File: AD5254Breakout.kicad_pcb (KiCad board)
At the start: 2 copper layers, 20.6 x 18 mm, 13 parts, among them J1 Conn_01x08, J2 Conn_01x08, U1 AD5254

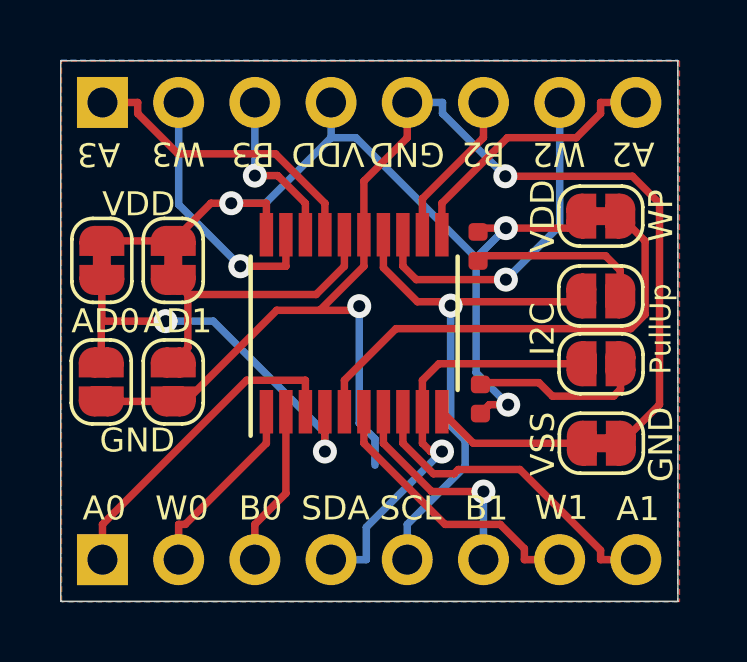
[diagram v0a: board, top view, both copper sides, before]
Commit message: Add condensor as Rev2021.05
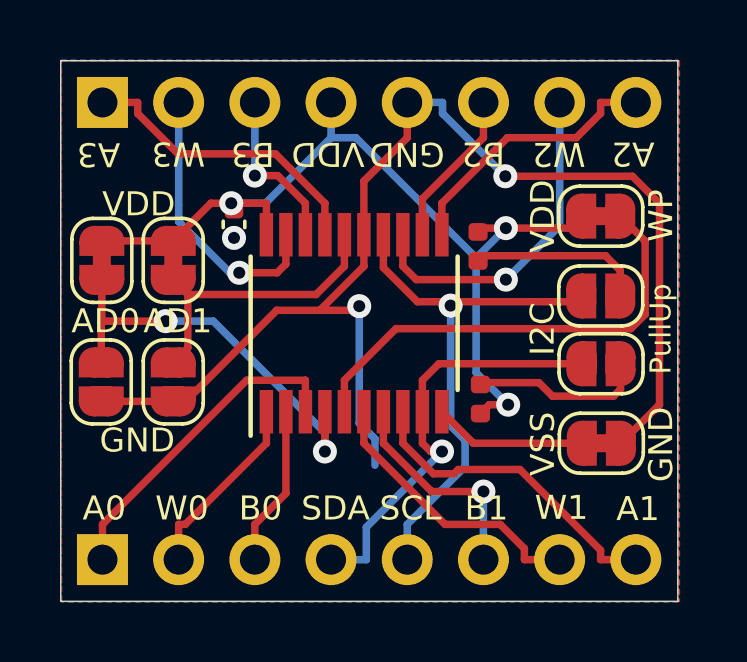
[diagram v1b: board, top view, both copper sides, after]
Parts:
- added C1: 0.1uf, Capacitor_SMD:C_0402_1005Metric, F.Cu at (155.9, 71.5)
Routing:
- net GND: vias 2 -> 3
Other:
- board text added: "Rev2021.05"
- board text removed: "Rev2019.11"
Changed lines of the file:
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@@
-(kicad_pcb (version 20171130) (host pcbnew 5.1.5-52549c5~84~ubuntu18.04.1)
+(kicad_pcb (version 20171130) (host pcbnew 5.1.10-88a1d61d58~88~ubuntu20.04.1)
   (general
     (thickness 1.6)
     (drawings 48)
-    (tracks 165)
+    (tracks 169)
     (zones 0)
-    (modules 13)
+    (modules 14)
     (nets 23)
   )
@@
     (add_net VDD)
   )
+  (module Capacitor_SMD:C_0402_1005Metric (layer F.Cu)
+    (at 155.875 71.475 270)
+    (descr "Capacitor SMD 0402 (1005 Metric), square (rectangular) end terminal, IPC_7351 nominal, (Body size source: IPC-SM-782 page 76, https://www.pcb-3d.com/wordpress/wp-content/uploads/ipc-sm-782a_amendment_1_and_2.pdf), generated with kicad-footprint-generator")
+    (tags capacitor)
+    (attr smd)
+    (fp_text reference C1 (at -1.325 0.075) (layer F.SilkS) hide
+      (effects (font (size 0.6 0.6) (thickness 0.15)))
+    )
+    (fp_text value 0.1uf (at 0 1.16 90) (layer F.Fab)
+      (effects (font (size 1 1) (thickness 0.15)))
+    )
+    (fp_line (start 0.91 0.46) (end -0.91 0.46) (layer F.CrtYd) (width 0.05))
+    (fp_line (start 0.91 -0.46) (end 0.91 0.46) (layer F.CrtYd) (width 0.05))
+    (fp_line (start -0.91 -0.46) (end 0.91 -0.46) (layer F.CrtYd) (width 0.05))
+    (fp_line (start -0.91 0.46) (end -0.91 -0.46) (layer F.CrtYd) (width 0.05))
+    (fp_line (start -0.107836 0.36) (end 0.107836 0.36) (layer F.SilkS) (width 0.12))
+    (fp_line (start -0.107836 -0.36) (end 0.107836 -0.36) (layer F.SilkS) (width 0.12))
+    (fp_line (start 0.5 0.25) (end -0.5 0.25) (layer F.Fab) (width 0.1))
+    (fp_line (start 0.5 -0.25) (end 0.5 0.25) (layer F.Fab) (width 0.1))
+    (fp_line (start -0.5 -0.25) (end 0.5 -0.25) (layer F.Fab) (width 0.1))
+    (fp_line (start -0.5 0.25) (end -0.5 -0.25) (layer F.Fab) (width 0.1))
+    (fp_text user %R (at 0 0 90) (layer F.Fab)
+      (effects (font (size 0.25 0.25) (thickness 0.04)))
+    )
+    (pad 2 smd roundrect (at 0.48 0 270) (size 0.56 0.62) (layers F.Cu F.Paste F.Mask) (roundrect_rratio 0.25)
+      (net 7 GND))
+    (pad 1 smd roundrect (at -0.48 0 270) (size 0.56 0.62) (layers F.Cu F.Paste F.Mask) (roundrect_rratio 0.25)
+      (net 4 VDD))
+    (model ${KISYS3DMOD}/Capacitor_SMD.3dshapes/C_0402_1005Metric.wrl
+      (at (xyz 0 0 0))
+      (scale (xyz 1 1 1))
+      (rotate (xyz 0 0 0))
+    )
+  )
   (module footprints:PinHeader_1x08_P2.54mm_Vertical_without_lines (layer F.Cu)
     (at 151.49 67.41 90)
@@
       (effects (font (size 1 1) (thickness 0.15)))
     )
-    (fp_text user %R (at 0 0 90) (layer F.Fab)
-      (effects (font (size 0.25 0.25) (thickness 0.04)))
-    )
     (fp_line (start 0.93 0.47) (end -0.93 0.47) (layer F.CrtYd) (width 0.05))
     (fp_line (start 0.93 -0.47) (end 0.93 0.47) (layer F.CrtYd) (width 0.05))
@@
     (fp_line (start -0.5 -0.25) (end 0.5 -0.25) (layer F.Fab) (width 0.1))
     (fp_line (start -0.5 0.25) (end -0.5 -0.25) (layer F.Fab) (width 0.1))
+    (fp_text user %R (at 0 0 90) (layer F.Fab)
+      (effects (font (size 0.25 0.25) (thickness 0.04)))
+    )
     (pad 2 smd roundrect (at 0.485 0 90) (size 0.59 0.64) (layers F.Cu F.Paste F.Mask) (roundrect_rratio 0.25)
       (net 4 VDD))
@@
       (effects (font (size 1 1) (thickness 0.15)))
     )
-    (fp_text user %R (at 0 0 90) (layer F.Fab)
-      (effects (font (size 0.25 0.25) (thickness 0.04)))
-    )
     (fp_line (start 0.93 0.47) (end -0.93 0.47) (layer F.CrtYd) (width 0.05))
     (fp_line (start 0.93 -0.47) (end 0.93 0.47) (layer F.CrtYd) (width 0.05))
@@
     (fp_line (start -0.5 -0.25) (end 0.5 -0.25) (layer F.Fab) (width 0.1))
     (fp_line (start -0.5 0.25) (end -0.5 -0.25) (layer F.Fab) (width 0.1))
+    (fp_text user %R (at 0 0 90) (layer F.Fab)
+      (effects (font (size 0.25 0.25) (thickness 0.04)))
+    )
     (pad 2 smd roundrect (at 0.485 0 270) (size 0.59 0.64) (layers F.Cu F.Paste F.Mask) (roundrect_rratio 0.25)
       (net 4 VDD))
@@
       (effects (font (size 1 1) (thickness 0.15)))
     )
-    (fp_text user %R (at 0 0 90) (layer F.Fab)
-      (effects (font (size 0.8 0.8) (thickness 0.15)))
-    )
     (fp_line (start -3.75 -3.45) (end 2.225 -3.45) (layer F.SilkS) (width 0.15))
     (fp_line (start -2.225 3.45) (end 2.225 3.45) (layer F.SilkS) (width 0.15))
@@
     (fp_line (start 2.2 -3.25) (end 2.2 3.25) (layer F.Fab) (width 0.15))
     (fp_line (start -1.2 -3.25) (end 2.2 -3.25) (layer F.Fab) (width 0.15))
+    (fp_text user %R (at 0 0 90) (layer F.Fab)
+      (effects (font (size 0.8 0.8) (thickness 0.15)))
+    )
     (pad 20 smd rect (at 2.95 -2.925 90) (size 1.45 0.45) (layers F.Cu F.Paste F.Mask)
       (net 4 VDD))
@@
       ))
   )
-  (gr_text Rev2019.11 (at 153.95 73.675 180) (layer B.SilkS)
+  (gr_text Rev2021.05 (at 153.95 73.675 180) (layer B.SilkS)
     (effects (font (size 0.8 0.8) (thickness 0.2)) (justify mirror))
   )
@@
   (segment (start 159.11 82.65) (end 160.2853 82.65) (width 0.25) (layer B.Cu) (net 6))
   (via (at 162.808 79.0465) (size 0.8) (layers F.Cu B.Cu) (net 6))
+  (via (at 155.875 71.925) (size 0.8) (drill 0.4) (layers F.Cu B.Cu) (net 7))
   (segment (start 153.85 77.375) (end 154.2602 77.375) (width 0.25) (layer F.Cu) (net 7))
   (segment (start 154.2602 77.375) (end 157.2973 74.3379) (width 0.25) (layer F.Cu) (net 7))
@@
   (segment (start 156.57 67.41) (end 156.57 69.8485) (width 0.25) (layer B.Cu) (net 15))
   (via (at 156.57 69.8485) (size 0.8) (layers F.Cu B.Cu) (net 15))
-  (segment (start 157.605 72.8703) (end 156.0848 72.8703) (width 0.25) (layer F.Cu) (net 16))
-  (segment (start 154.03 67.41) (end 154.03 70.8155) (width 0.25) (layer B.Cu) (net 16))
-  (segment (start 154.03 70.8155) (end 156.0848 72.8703) (width 0.25) (layer B.Cu) (net 16))
-  (segment (start 157.605 71.82) (end 157.605 72.8703) (width 0.25) (layer F.Cu) (net 16))
-  (via (at 156.0848 72.8703) (size 0.8) (layers F.Cu B.Cu) (net 16))
+  (via (at 156.05 73.0872) (size 0.8) (drill 0.4) (layers F.Cu B.Cu) (net 16))
+  (segment (start 157.3128 73.0872) (end 156.05 73.0872) (width 0.25) (layer F.Cu) (net 16))
+  (segment (start 157.605 72.795) (end 157.3128 73.0872) (width 0.25) (layer F.Cu) (net 16))
+  (segment (start 157.605 71.82) (end 157.605 72.795) (width 0.25) (layer F.Cu) (net 16))
+  (segment (start 154.03 70.8155) (end 154.03 67.41) (width 0.25) (layer B.Cu) (net 16))
+  (segment (start 154.03 71.381185) (end 154.03 70.8155) (width 0.25) (layer B.Cu) (net 16))
+  (segment (start 155.736015 73.0872) (end 154.03 71.381185) (width 0.25) (layer B.Cu) (net 16))
+  (segment (start 156.05 73.0872) (end 155.736015 73.0872) (width 0.25) (layer B.Cu) (net 16))
   (segment (start 158.905 70.7697) (end 157.2585 69.1232) (width 0.25) (layer F.Cu) (net 17))
   (segment (start 157.2585 69.1232) (end 154.0111 69.1232) (width 0.25) (layer F.Cu) (net 17))

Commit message: Update for KiCad6
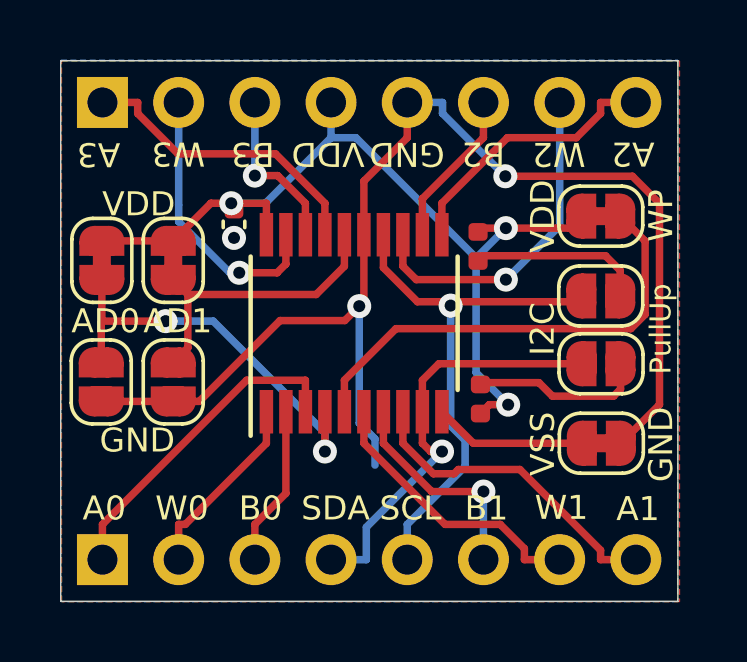
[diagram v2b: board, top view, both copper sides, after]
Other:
- net class Default removed
